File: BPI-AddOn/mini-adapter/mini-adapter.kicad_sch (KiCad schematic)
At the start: 12 parts, among them J1 RJ45, J3 MS2 Kabel, J4 Grove, J5 RJ45, P1 DIN10-1, P2 DIN7-1, P3 CONN_01X05, P4 CAN Term

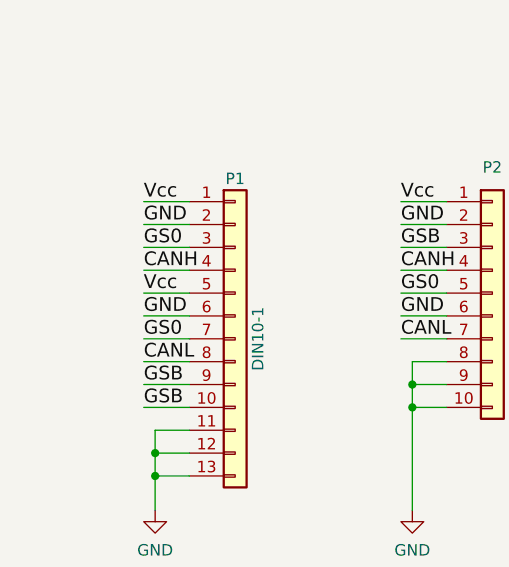
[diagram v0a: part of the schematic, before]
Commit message: add MS1 Slave / Pin 5 Vcc
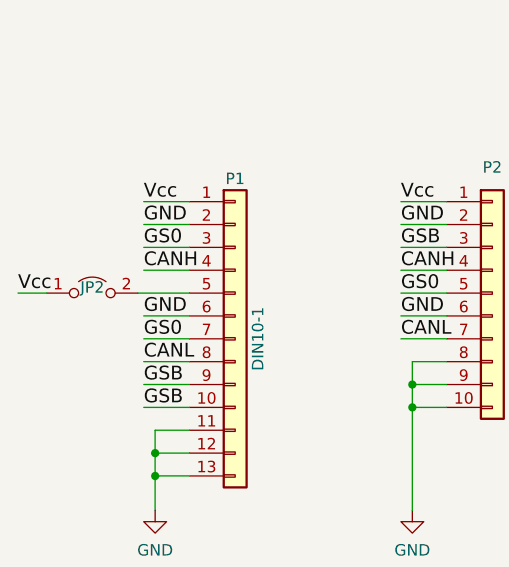
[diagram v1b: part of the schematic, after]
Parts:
- added JP2: MS1 Slave, Connector_PinHeader_2.54mm:PinHeader_1x02_P2.54mm_Vertical, symbol Jumper:Jumper_2_Open
- J4: footprint Maerklin:Grove_1x04 -> Connector_JST:JST_PH_B4B-PH-K_1x04_P2.00mm_Vertical
- R1, R2: footprint Resistor_THT:R_Axial_DIN0204_L3.6mm_D1.6mm_P5.08mm_Horizontal -> Resistor_THT:R_Axial_DIN0204_L3.6mm_D1.6mm_P7.62mm_Horizontal
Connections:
- net Vcc: now also JP2.1 (A); no longer P1.5 (Pin_5)
- new net: JP2.2 (B), P1.5 (Pin_5)
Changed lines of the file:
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@@
-    (stroke (width 0) (type default) (color 0 0 0 0))
-  )
-  (wire (pts (xy 74.295 107.315) (xy 79.375 107.315))
     (stroke (width 0) (type default) (color 0 0 0 0))
   )
@@
     (stroke (width 0) (type default) (color 0 0 0 0))
   )
+  (wire (pts (xy 73.66 107.315) (xy 79.375 107.315))
+    (stroke (width 0) (type default) (color 0 0 0 0))
+  )
   (wire (pts (xy 128.27 118.745) (xy 133.35 118.745))
     (stroke (width 0) (type default) (color 0 0 0 0))
@@
   )
   (wire (pts (xy 75.565 127.635) (xy 75.565 131.445))
+    (stroke (width 0) (type default) (color 0 0 0 0))
+  )
+  (wire (pts (xy 60.325 107.315) (xy 63.5 107.315))
     (stroke (width 0) (type default) (color 0 0 0 0))
   )
@@
     (effects (font (size 1.524 1.524)) (justify left bottom))
   )
-  (label "Vcc" (at 74.295 107.315 0)
+  (label "Vcc" (at 60.325 107.315 0)
     (effects (font (size 1.524 1.524)) (justify left bottom))
   )
@@
     (property "Reference" "J4" (id 0) (at 146.685 129.54 0))
     (property "Value" "Grove" (id 1) (at 149.225 125.73 0))
-    (property "Footprint" "Maerklin:Grove_1x04" (id 2) (at 144.145 130.81 0)
+    (property "Footprint" "Connector_JST:JST_PH_B4B-PH-K_1x04_P2.00mm_Vertical" (id 2) (at 144.145 130.81 0)
       (effects (font (size 1.27 1.27)) hide)
     )
@@
     (pin "1")
   )
+  (symbol (lib_id "Jumper:Jumper_2_Open") (at 68.58 107.315 0) (unit 1)
+    (in_bom yes) (on_board yes)
+    (property "Reference" "JP2" (id 0) (at 68.58 106.68 0))
+    (property "Value" "MS1 Slave" (id 1) (at 68.58 103.6574 0)
+      (effects (font (size 1.27 1.27)) hide)
+    )
+    (property "Footprint" "Connector_PinHeader_2.54mm:PinHeader_1x02_P2.54mm_Vertical" (id 2) (at 68.58 107.315 0)
+      (effects (font (size 1.27 1.27)) hide)
+    )
+    (property "Datasheet" "~" (id 3) (at 68.58 107.315 0)
+      (effects (font (size 1.27 1.27)) hide)
+    )
+    (pin "1")
+    (pin "2")
+  )
   (symbol (lib_id "Connector_Generic:Conn_01x13") (at 84.455 112.395 0) (unit 1)
     (in_bom yes) (on_board yes)
@@
       (effects (font (size 1.27 1.27)) (justify left))
     )
-    (property "Footprint" "Resistor_THT:R_Axial_DIN0204_L3.6mm_D1.6mm_P5.08mm_Horizontal" (id 2) (at 131.572 100.965 90)
+    (property "Footprint" "Resistor_THT:R_Axial_DIN0204_L3.6mm_D1.6mm_P7.62mm_Horizontal" (id 2) (at 131.572 100.965 90)
       (effects (font (size 1.27 1.27)) hide)
     )
@@
     (property "Reference" "R2" (id 0) (at 163.195 90.17 90))
     (property "Value" "8k2" (id 1) (at 163.195 92.71 90))
-    (property "Footprint" "Resistor_THT:R_Axial_DIN0204_L3.6mm_D1.6mm_P5.08mm_Horizontal" (id 2) (at 163.195 94.488 90)
+    (property "Footprint" "Resistor_THT:R_Axial_DIN0204_L3.6mm_D1.6mm_P7.62mm_Horizontal" (id 2) (at 163.195 94.488 90)
       (effects (font (size 1.27 1.27)) hide)
     )
@@
     )
     (path "/06a98dcd-269e-4c39-9ee1-de4996f59e9b"
-      (reference "J4") (unit 1) (value "Grove") (footprint "Maerklin:Grove_1x04")
+      (reference "J4") (unit 1) (value "Grove") (footprint "Connector_JST:JST_PH_B4B-PH-K_1x04_P2.00mm_Vertical")
     )
     (path "/80242ded-39ea-4c7a-bf87-ce9ebe416501"
@@
       (reference "JP1") (unit 1) (value "5V") (footprint "Connector_PinHeader_2.54mm:PinHeader_1x02_P2.54mm_Vertical")
     )
+    (path "/42594506-dfaa-4fbf-9cfd-7bc8bb436674"
+      (reference "JP2") (unit 1) (value "MS1 Slave") (footprint "Connector_PinHeader_2.54mm:PinHeader_1x02_P2.54mm_Vertical")
+    )
     (path "/57d36429-653e-430a-8f5a-a444bf8d1ed5"
       (reference "P1") (unit 1) (value "DIN10-1") (footprint "Maerklin:minidin-10")
@@
     )
     (path "/a9a3bb8a-8635-4317-adbc-5266d9efc9bb"
-      (reference "R1") (unit 1) (value "120") (footprint "Resistor_THT:R_Axial_DIN0204_L3.6mm_D1.6mm_P5.08mm_Horizontal")
+      (reference "R1") (unit 1) (value "120") (footprint "Resistor_THT:R_Axial_DIN0204_L3.6mm_D1.6mm_P7.62mm_Horizontal")
     )
     (path "/b27699cd-2e5f-4862-9b5a-5b0ee9ef985c"
-      (reference "R2") (unit 1) (value "8k2") (footprint "Resistor_THT:R_Axial_DIN0204_L3.6mm_D1.6mm_P5.08mm_Horizontal")
-    )
-  )
+      (reference "R2") (unit 1) (value "8k2") (footprint "Resistor_THT:R_Axial_DIN0204_L3.6mm_D1.6mm_P7.62mm_Horizontal")
+    )
+  )

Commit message: rename JP2 to MS1 Master
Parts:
- JP2: value MS1 Slave -> MS1 Master
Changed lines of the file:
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@@
     (in_bom yes) (on_board yes)
     (property "Reference" "JP2" (id 0) (at 68.58 106.68 0))
-    (property "Value" "MS1 Slave" (id 1) (at 68.58 103.6574 0)
+    (property "Value" "MS1 Master" (id 1) (at 68.58 103.6574 0)
       (effects (font (size 1.27 1.27)) hide)
     )
@@
     )
     (path "/42594506-dfaa-4fbf-9cfd-7bc8bb436674"
-      (reference "JP2") (unit 1) (value "MS1 Slave") (footprint "Connector_PinHeader_2.54mm:PinHeader_1x02_P2.54mm_Vertical")
+      (reference "JP2") (unit 1) (value "MS1 Master") (footprint "Connector_PinHeader_2.54mm:PinHeader_1x02_P2.54mm_Vertical")
     )
     (path "/57d36429-653e-430a-8f5a-a444bf8d1ed5"

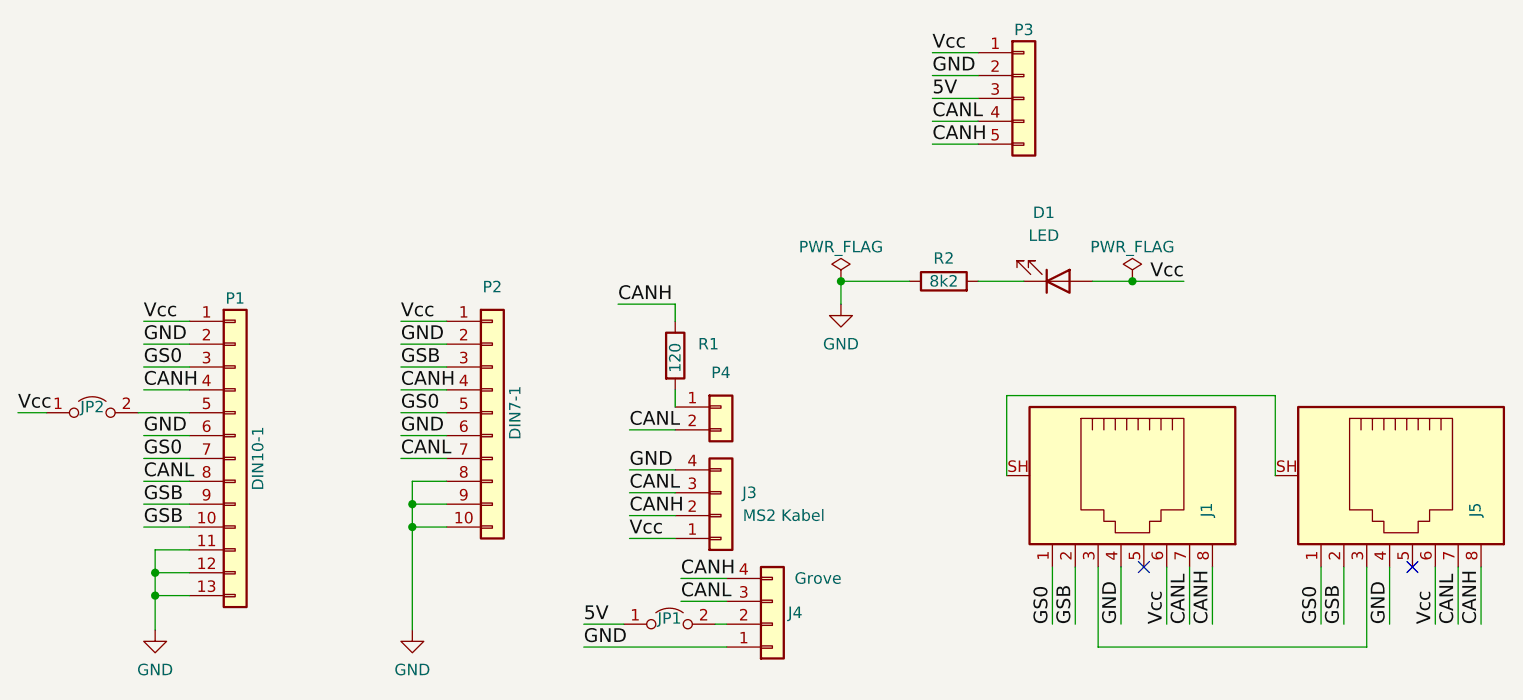
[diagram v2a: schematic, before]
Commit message: move some description on the silkscreen
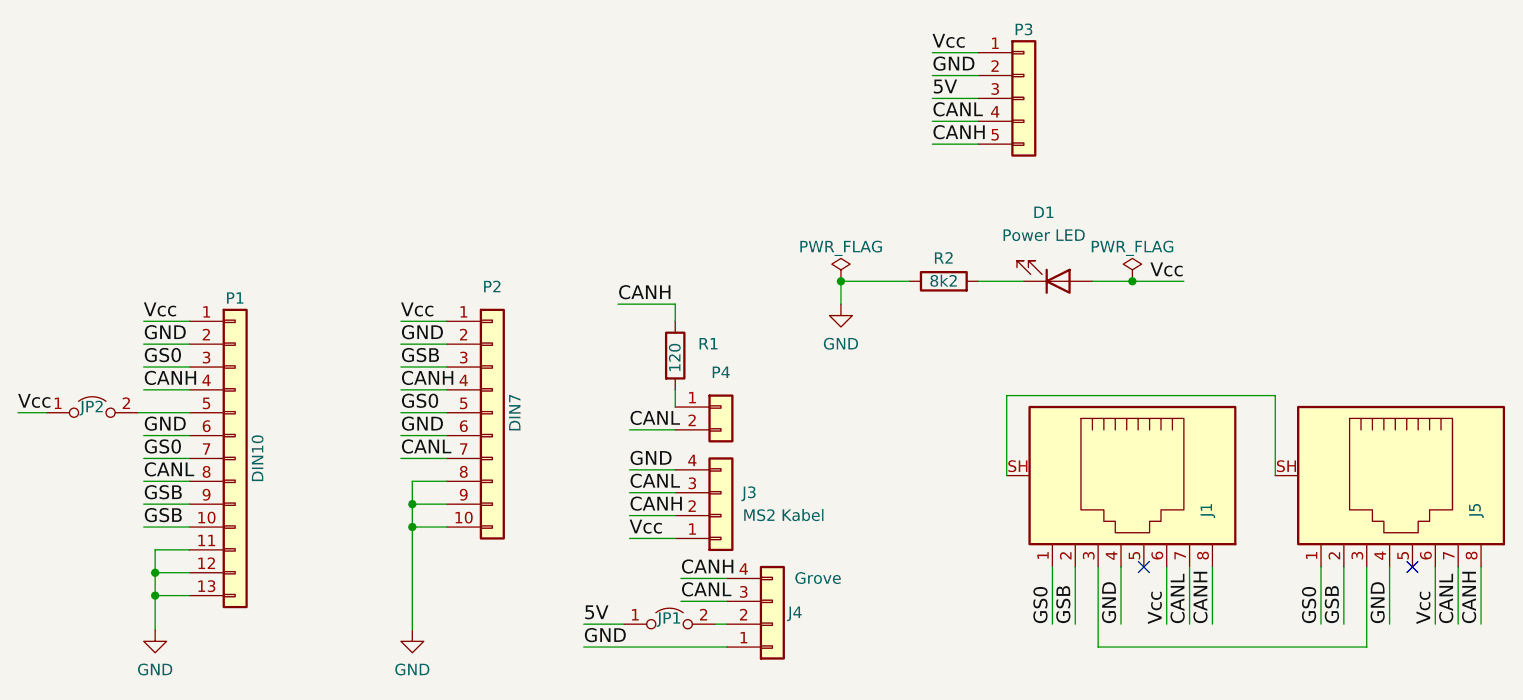
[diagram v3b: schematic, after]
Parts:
- D1: value LED -> Power LED
- P1: value DIN10-1 -> DIN10
- P2: value DIN7-1 -> DIN7
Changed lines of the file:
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@@
     (in_bom yes) (on_board yes)
     (property "Reference" "P1" (id 0) (at 84.455 94.615 0))
-    (property "Value" "DIN10-1" (id 1) (at 86.995 112.395 90))
+    (property "Value" "DIN10" (id 1) (at 86.995 112.395 90))
     (property "Footprint" "Maerklin:minidin-10" (id 2) (at 84.455 112.395 0)
       (effects (font (size 1.27 1.27)) hide)
@@
     (in_bom yes) (on_board yes) (fields_autoplaced)
     (property "Reference" "D1" (id 0) (at 174.3075 85.09 0))
-    (property "Value" "LED" (id 1) (at 174.3075 87.63 0))
+    (property "Value" "Power LED" (id 1) (at 174.3075 87.63 0))
     (property "Footprint" "LED_THT:LED_D3.0mm" (id 2) (at 175.895 92.71 0)
       (effects (font (size 1.27 1.27)) hide)
@@
     (in_bom yes) (on_board yes)
     (property "Reference" "P2" (id 0) (at 113.03 93.345 0))
-    (property "Value" "DIN7-1" (id 1) (at 115.57 107.315 90))
+    (property "Value" "DIN7" (id 1) (at 115.57 107.315 90))
     (property "Footprint" "Maerklin:minidin-7" (id 2) (at 113.03 107.315 0)
       (effects (font (size 1.27 1.27)) hide)
@@
     )
     (path "/ba0f68a3-6a99-4ade-9d51-66f7575b6b96"
-      (reference "D1") (unit 1) (value "LED") (footprint "LED_THT:LED_D3.0mm")
+      (reference "D1") (unit 1) (value "Power LED") (footprint "LED_THT:LED_D3.0mm")
     )
     (path "/1e003465-66d8-485e-8650-954bf7b058b8"
@@
     )
     (path "/57d36429-653e-430a-8f5a-a444bf8d1ed5"
-      (reference "P1") (unit 1) (value "DIN10-1") (footprint "Maerklin:minidin-10")
+      (reference "P1") (unit 1) (value "DIN10") (footprint "Maerklin:minidin-10")
     )
     (path "/befbda66-d1f9-40de-9562-869338a0105f"
-      (reference "P2") (unit 1) (value "DIN7-1") (footprint "Maerklin:minidin-7")
+      (reference "P2") (unit 1) (value "DIN7") (footprint "Maerklin:minidin-7")
     )
     (path "/b120c146-20b4-4b2d-89b8-adaae128194a"
